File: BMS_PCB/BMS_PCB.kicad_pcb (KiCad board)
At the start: 2 copper layers, 163 parts, among them IC1 TPS560430XFDBVT, IC3 AMC1350DWVR, IC4 AMC1350DWVR, IC5 AMC1350DWVR, IC6 AMC1350DWVR, J1 Conn_01x37, J2 Conn_01x09, K1 Relay_SPST-NO, Q1 2N7002KT7G, U1 TLV2404IDR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

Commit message: Update BMS_PCB.kicad_pcb
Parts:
- moved J1 5.75 mm to (212.9, 130.6), turned to 90 degrees

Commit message: test
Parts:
- moved J1 99.5 mm to (239.2, 34.6)
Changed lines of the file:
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@@
 	(footprint "Connector_Dsub:DSUB-37_Socket_Horizontal_P2.77x2.84mm_EdgePinOffset14.56mm_Housed_MountingHolesOffset15.98mm"
 		(layer "F.Cu")
-		(at 212.925 130.58 90)
+		(at 239.159669 34.575 90)
 		(descr "37-pin D-Sub connector, horizontal/angled (90 deg), THT-mount, socket (female), pitch 2.77x2.84mm, pin-PCB-offset 14.56mm, distance of mounting holes 63.5mm, distance of mounting holes to PCB edge 15.98mm, see https://disti-assets.s3.amazonaws.com/tonar/files/datasheets/16730.pdf")
 		(tags "37-pin D-Sub connector horizontal angled 90deg THT socket pitch 2.77x2.84mm pin-PCB-offset 14.56mm mounting-holes-distance 63.5mm mounting-hole-offset 15.98mm")

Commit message: Update BMS_PCB.kicad_pcb
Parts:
- moved F5 93.1 mm to (271.0, 49.0), turned to 90 degrees
- moved R1 72.0 mm to (244.7, 70.3), turned to 180 degrees
- moved C18 71.0 mm to (273.0, 40.5), turned to 90 degrees
- moved C21 70.6 mm to (270.6, 31.0), turned to 180 degrees
- moved L1 68.7 mm to (271.0, 35.5), turned to 90 degrees
- moved C11 68.6 mm to (241.7, 65.3), turned to 90 degrees
- moved C19 68.2 mm to (270.0, 40.5), turned to 90 degrees
- moved C14 68.1 mm to (242.0, 77.9), turned to 90 degrees
- moved C5 67.8 mm to (241.8, 71.5), turned to -90 degrees
- moved PS1 67.6 mm to (253.5, 42.0), turned to 180 degrees
- moved R2 67.0 mm to (244.8, 72.5), turned to 180 degrees
- moved R8 66.8 mm to (244.7, 66.3), turned to 180 degrees
- moved R6 66.7 mm to (244.7, 64.3), turned to 180 degrees
- moved C1 65.1 mm to (239.0, 68.0)
- moved R10 62.8 mm to (239.7, 65.3), turned to 90 degrees
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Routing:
- net +BATT: track 0.00 -> 96.2 mm
- net -BATT: track 0.00 -> 58.0 mm
- net 12V_DCDC: track 0.00 -> 51.0 mm
- net Net-(PS1--VIN): track 0.00 -> 40.0 mm
- net Net-(PS1-+VIN): track 0.00 -> 14.5 mm
- net Net-(U1C-+): track 0.00 -> 10.1 mm
- net Net-(U1D-+): track 0.00 -> 10.1 mm
- net Net-(U1A-+): track 0.00 -> 9.40 mm
- net Net-(U2A-+): track 0.00 -> 9.40 mm
- net Net-(U2B-+): track 0.00 -> 9.22 mm
- net Net-(U1B-+): track 0.00 -> 9.03 mm
- net Relais_in+: track 0.00 -> 8.04 mm
- net +5V: track 0.00 -> 5.84 mm
- net Net-(U1C--): track 0.00 -> 4.94 mm
- net Net-(U1D--): track 0.00 -> 4.79 mm
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
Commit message: Freitag
Ich habe heute viele Bauteile zusammengesetzt. Die Leiterbahnen würde ich eher zum Schluss machen.
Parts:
- moved C2 146.6 mm to (210.8, 100.1), turned to 90 degrees
- moved C4 144.9 mm to (210.3, 107.1), turned to -90 degrees
- moved C15 142.9 mm to (210.8, 129.5), turned to 90 degrees
- moved C16 141.5 mm to (210.3, 137.1), turned to -90 degrees
- moved C6 140.8 mm to (205.3, 107.1), turned to 90 degrees
- moved C43 139.8 mm to (210.8, 114.6), turned to 90 degrees
- moved C44 138.2 mm to (210.3, 122.0), turned to -90 degrees
- moved C10 137.2 mm to (199.8, 107.1), turned to -90 degrees
- moved C17 137.0 mm to (205.3, 137.1), turned to 90 degrees
- moved C47 134.6 mm to (205.3, 122.0), turned to 90 degrees
- moved C63 132.2 mm to (210.8, 144.5), turned to 90 degrees
- moved C8 131.2 mm to (194.3, 107.1), turned to 90 degrees
- moved C64 131.1 mm to (210.3, 152.1), turned to -90 degrees
- moved C49 130.7 mm to (199.8, 122.1), turned to -90 degrees
- moved C12 128.4 mm to (189.3, 107.1), turned to 90 degrees
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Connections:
- K1 pad 1: (no net) -> Net-(K1-Pad14)
- K1 pad 2: (no net) -> Net-(D2-A)
- K1 pad 4: (no net) -> Precharge_out
- K1 pad 5: (no net) -> +5V
- K1 pad 6: (no net) -> Net-(K1-Pad14)
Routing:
- net GND: track 0.14 -> 38.3 mm
- net Net-(D2-A): track 0.00 -> 19.7 mm
- net Net-(U11A--): track 0.00 -> 16.8 mm
- net Net-(U11B--): track 0.00 -> 16.2 mm
- net Current: track 0.00 -> 16.1 mm
- net Net-(U11B-+): track 0.00 -> 12.3 mm
- net Net-(U11A-+): track 0.00 -> 12.1 mm
- net Net-(U8--): track 0.00 -> 10.9 mm
- net +5V: track 5.84 -> 16.5 mm
- net Net-(U8-+): track 0.00 -> 7.71 mm
- net Net-(Q1-G): track 0.00 -> 5.83 mm
- net Precharge_uC: track 0.00 -> 5.62 mm
- net Vcc_Current: track 0.00 -> 4.82 mm
- net Net-(C51-Pad2): track 0.00 -> 3.09 mm
- net Net-(C31-Pad2): track 0.00 -> 3.09 mm

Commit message: Sonntag
Ich habe das Layout weitergemacht, die restlichen Schaltungen zusammengestellt und das meiste bereits verbunden.  Problem sind noch die PS-Boxen (R1SE-0505-R), die für die Voltage Messung noch angeschlossen werden müssen. da müssen wir schauen, wie wir die platztechnisch platzieren.
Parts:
- moved PS6 166.6 mm to (205.2, 93.6)
- moved C59 161.9 mm to (194.5, 93.0), turned to -90 degrees
- moved U10 154.7 mm to (224.2, 50.5)
- moved PS5 153.2 mm to (205.2, 76.9)
- moved C55 149.9 mm to (194.5, 77.4), turned to -90 degrees
- moved PS4 143.9 mm to (205.2, 60.4)
- moved C53 142.9 mm to (194.5, 60.5), turned to -90 degrees
- moved C52 139.0 mm to (194.5, 45.5), turned to -90 degrees
- moved PS3 138.8 mm to (205.2, 44.0)
- moved J2 105.9 mm to (141.9, 130.2)
- moved U7 88.7 mm to (153.5, 72.5)
- moved C39 85.0 mm to (196.8, 131.0)
- moved C40 75.7 mm to (190.2, 147.5), turned to 90 degrees
- moved IC1 64.0 mm to (226.3, 35.0)
- moved C42 62.2 mm to (175.0, 134.0), turned to 90 degrees
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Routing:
- net GND: track 38.3 -> 169.1 mm
- net +5V: track 16.5 -> 86.7 mm
- net Net-(U3A--): track 0.00 -> 55.5 mm
- net Net-(U3A-+): track 0.00 -> 47.2 mm
- net Voltage1: track 0.00 -> 43.8 mm
- net Voltage3: track 0.00 -> 43.3 mm
- net Voltage2: track 0.00 -> 42.0 mm
- net Net-(U3B-+): track 0.00 -> 31.0 mm
- net Net-(U3B--): track 0.00 -> 30.3 mm
- net Net-(U3D-+): track 0.00 -> 28.0 mm
- net Voltage0: track 0.00 -> 27.7 mm
- net Net-(U3C--): track 0.00 -> 26.8 mm
- net Net-(U3C-+): track 0.00 -> 25.8 mm
- net Voltage23_uC: track 0.00 -> 25.6 mm
- net Net-(C31-Pad2): track 3.09 -> 27.9 mm
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
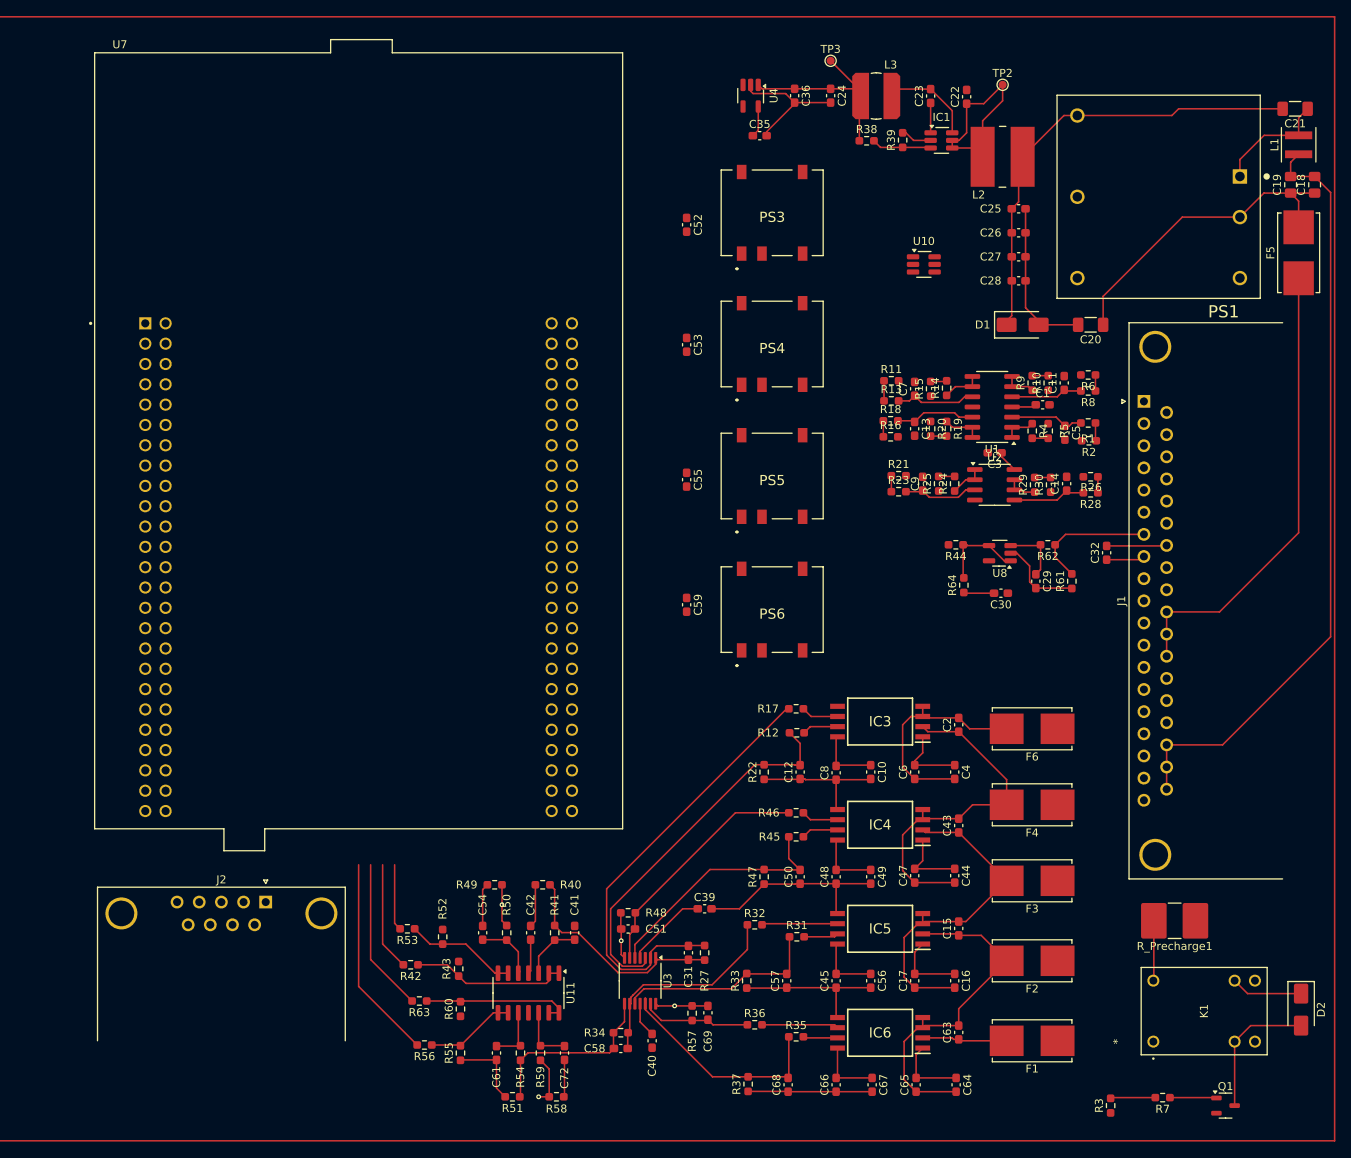
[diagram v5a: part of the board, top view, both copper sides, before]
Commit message: Montag, 28.04.
Pin Belegung PCB geändert, noch nicht in Schematics
PS-Boxen platziert
80 % fertig verteilt und verbunden
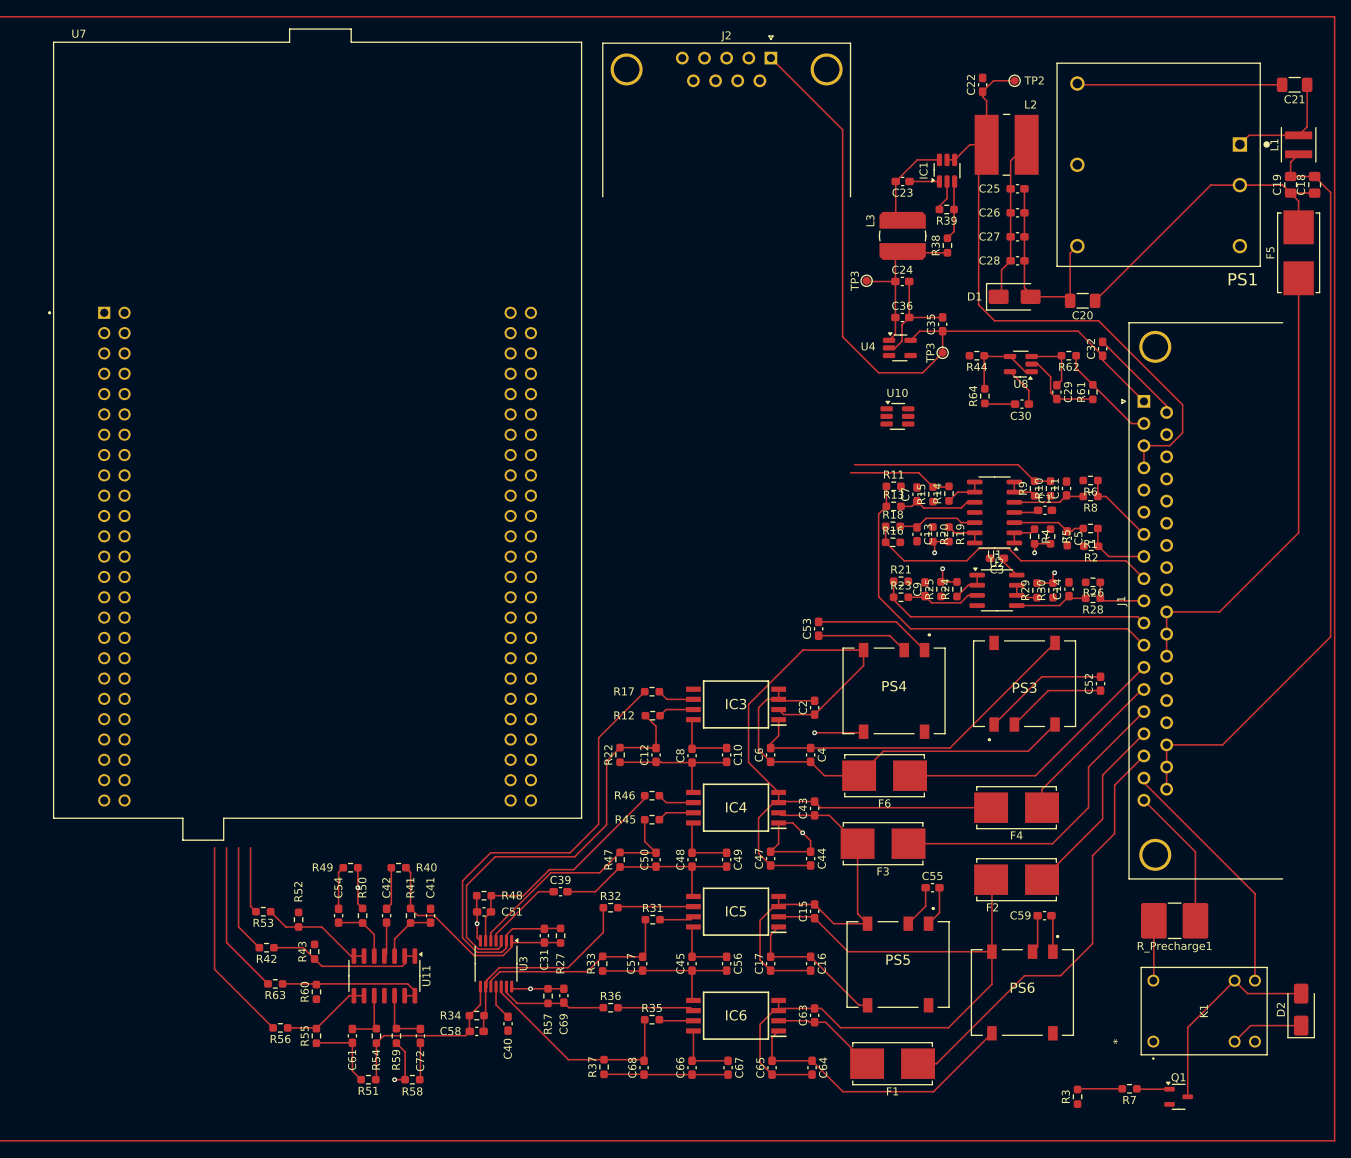
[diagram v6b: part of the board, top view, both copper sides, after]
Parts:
- added TP3: TestPoint, TestPoint:TestPoint_Pad_D1.0mm, F.Cu at (226.5, 61.5)
- moved J2 123.0 mm to (205.0, 24.7)
- moved C52 77.2 mm to (246.2, 102.9), turned to 90 degrees
- moved PS3 66.8 mm to (236.7, 102.9)
- moved PS5 63.1 mm to (220.9, 138.0), turned to 180 degrees
- moved C55 59.5 mm to (225.2, 128.4), turned to 0 degrees
- moved C59 59.3 mm to (239.2, 131.9), turned to 0 degrees
- moved PS6 57.2 mm to (236.5, 141.5), turned to 180 degrees
- moved PS4 46.0 mm to (220.4, 103.8), turned to 180 degrees
- moved C53 39.1 mm to (211.0, 96.0), turned to 90 degrees
- moved U4 36.6 mm to (221.2, 60.9), turned to 0 degrees
- moved C35 32.8 mm to (226.5, 57.9), turned to 90 degrees
- moved C36 30.8 mm to (221.5, 57.1), turned to 0 degrees
- moved TP3 27.9 mm to (217.0, 52.5), turned to 90 degrees
- moved C32 25.5 mm to (246.5, 61.0)
- moved C24 24.9 mm to (221.5, 52.6), turned to 0 degrees
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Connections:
- F1 pad 1: Net-(J1-Pin_13) -> Net-(J1-Pin_17)
- F2 pad 1: Net-(J1-Pin_12) -> Net-(J1-Pin_16)
- F3 pad 1: Net-(J1-Pin_11) -> Net-(J1-Pin_15)
- F4 pad 1: Net-(J1-Pin_10) -> Net-(J1-Pin_14)
- F6 pad 1: Net-(J1-Pin_9) -> Net-(J1-Pin_13)
- J1 pad 1: Temp1 -> Vcc_Current
- J1 pad 10: Net-(J1-Pin_10) -> Temp6
- J1 pad 11: Net-(J1-Pin_11) -> Temp5
- J1 pad 12: Net-(J1-Pin_12) -> Temp3
- J1 pad 14: Precharge_out -> Net-(J1-Pin_14)
- J1 pad 15: Precharge_in -> Net-(J1-Pin_15)
- J1 pad 16: Relais_out+ -> Net-(J1-Pin_16)
- J1 pad 17: Relais_in+ -> Net-(J1-Pin_17)
- J1 pad 18: Relais_out- -> Precharge_out
- J1 pad 19: Relais_in+ -> Precharge_in
- J1 pad 2: Temp2 -> Current
- J1 pad 3: Temp3 -> Relais_in+
- J1 pad 4: Temp4 -> Relais_in+
- J1 pad 5: Temp5 -> Relais_out+
- J1 pad 6: Temp6 -> Relais_out-
- J1 pad 7: Current -> Temp2
- J1 pad 8: Vcc_Current -> Temp1
- J1 pad 9: Net-(J1-Pin_9) -> Temp4
- K1 pad 2: Net-(D2-A) -> +5V
- K1 pad 5: +5V -> Net-(D2-A)
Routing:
- net Vcc_Current: track 8.75 -> 90.2 mm
- net Relais_in+: track 26.6 -> 81.6 mm
- net Net-(J1-Pin_17): track 0.00 -> 54.2 mm
- net GND: track 169.1 -> 216.6 mm
- net Temp3: track 2.51 -> 49.9 mm
- net Voltage3: track 43.3 -> 87.8 mm
- net Voltage1: track 43.8 -> 88.2 mm
- net Net-(J1-Pin_15): track 0.00 -> 39.2 mm
- net +5V_Bat0: track 8.96 -> 45.0 mm
- net Temp4: track 2.00 -> 37.4 mm
- net Net-(J1-Pin_13): track 0.00 -> 34.8 mm
- net +5V: track 86.7 -> 121.5 mm
- net Temp5: track 2.00 -> 34.8 mm
- net Precharge_out: track 0.00 -> 31.1 mm
- net Voltage0: track 27.7 -> 55.1 mm
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
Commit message: Footprints changes
-U10
-uC pins/SPI changes
- Fuses
- DSUB
- reupload layout
- etc.
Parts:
- removed the TP3 at (217.0, 52.5)
- removed the TP3 at (226.5, 61.5)
- added R65: DUMMY, Resistor_SMD:R_0603_1608Metric_Pad0.98x0.95mm_HandSolder, F.Cu at (72.7, 65.2)
- added TP1: TestPoint, TestPoint:TestPoint_Pad_D1.0mm, F.Cu at (72.0, 70.0)
- added TP3: TestPoint, TestPoint:TestPoint_Pad_D1.0mm, F.Cu at (72.0, 57.0)
- C22: value 2,2u -> 2u2
- F1, F2, F3, F4, F6: value 1A -> 100mA; footprint Fuse:Fuseholder_Littelfuse_Nano2_154x -> Fuse:Fuse_Littelfuse-NANO2-451_453
- J2: value Conn_01x09 -> Conn_01x15; footprint Connector_Dsub:DSUB-9_Socket_Horizontal_P2.77x2.84mm_EdgePinOffset14.56mm_Housed_MountingHolesOffset15.98mm -> Connector_Dsub:DSUB-15_Socket_Horizontal_P2.77x2.84mm_EdgePinOffset14.56mm_Housed_MountingHolesOffset15.98mm
- K1: value Relay_SPST-NO -> J1021AS35VDC.20
- R44: value 1k -> 100
- U10: footprint Package_TO_SOT_SMD:SOT-23-6_Handsoldering -> Package_SO:SOIC-16_3.9x9.9mm_P1.27mm
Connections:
- F1 pad 1: Net-(J1-Pin_17) -> Net-(J1-Pin_13)
- F2 pad 1: Net-(J1-Pin_16) -> Net-(J1-Pin_12)
- F3 pad 1: Net-(J1-Pin_15) -> Net-(J1-Pin_11)
- F4 pad 1: Net-(J1-Pin_14) -> Net-(J1-Pin_10)
- F6 pad 1: Net-(J1-Pin_13) -> Net-(J1-Pin_9)
- J1 pad 1: Vcc_Current -> Temp1
- J1 pad 10: Temp6 -> Net-(J1-Pin_10)
- J1 pad 11: Temp5 -> Net-(J1-Pin_11)
- J1 pad 12: Temp3 -> Net-(J1-Pin_12)
- J1 pad 14: Net-(J1-Pin_14) -> Precharge_out
- J1 pad 15: Net-(J1-Pin_15) -> Precharge_in
- J1 pad 16: Net-(J1-Pin_16) -> Relais_out+
- J1 pad 17: Net-(J1-Pin_17) -> Relais_in+
- J1 pad 18: Precharge_out -> Relais_out-
- J1 pad 19: Precharge_in -> Relais_in+
- J1 pad 2: Current -> Temp2
- J1 pad 3: Relais_in+ -> Temp3
- J1 pad 4: Relais_in+ -> Temp4
- J1 pad 5: Relais_out+ -> Temp5
- J1 pad 6: Relais_out- -> Temp6
- J1 pad 7: Temp2 -> Current
- J1 pad 8: Temp1 -> Vcc_Current
- J1 pad 9: Temp4 -> Net-(J1-Pin_9)
- J2 pad 8: unconnected-(J2-Pin_8-Pad8) -> Touchdisplay_x
- J2 pad 9: unconnected-(J2-Pin_9-Pad9) -> Touchdisplay_y
- K1 pad 1: Net-(K1-Pad14) -> Net-(K1-Pad1)
- K1 pad 3: (no net) -> unconnected-(K1-Pad3)
- K1 pad 6: Net-(K1-Pad14) -> unconnected-(K1-Pad6)
- R44 pad 1: Net-(U8--) -> Net-(R44-Pad1)
- R64 pad 2: Net-(U8--) -> Net-(R44-Pad1)
- R_Precharge1 pad 2: Net-(K1-Pad14) -> Net-(K1-Pad1)
- U7 pad P1_18: unconnected-(U7A-PA6-PadP1_18) -> Touchdisplay_x
- U7 pad P1_19: Current_uC -> Temp3_uC
- U7 pad P1_7: Temp3_uC -> Current_uC
- U7 pad P1_8: unconnected-(U7A-PC0-PadP1_8) -> Touchdisplay_y
- U7 pad P2_11: unconnected-(U7B-PE6-PadP2_11) -> Touchdisplay_y-
- U7 pad P2_13: unconnected-(U7B-PE4-PadP2_13) -> Touchdisplay_x-
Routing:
- net (no net): track 0.00 -> 146.7 mm
- net Net-(J1-Pin_17): track 54.2 -> 0.00 mm
- net Net-(J1-Pin_15): track 39.2 -> 0.00 mm
- net Net-(J1-Pin_16): track 23.8 -> 0.00 mm
- net Net-(J1-Pin_14): track 22.0 -> 0.00 mm
- net Net-(K1-Pad14): track 7.51 -> 0.00 mm

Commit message: Dienstag, 29.04.
Layout soweit fertig gestellt, Probleme noch mit Footprints
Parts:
- moved TP3 162.0 mm to (234.0, 57.5), turned to 90 degrees
- moved TP1 147.0 mm to (218.5, 57.5)
- moved R65 136.0 mm to (208.5, 72.1), turned to 180 degrees
- moved J2 46.5 mm to (250.7, 33.8), turned to 90 degrees
- moved IC1 36.8 mm to (198.9, 62.5), turned to 180 degrees
- moved L2 32.5 mm to (202.0, 37.0)
- moved C21 31.7 mm to (239.0, 31.5)
- moved C18 31.6 mm to (241.5, 42.0)
- moved C19 31.6 mm to (238.5, 42.0)
- moved C20 31.6 mm to (212.5, 56.5)
- moved C25 31.6 mm to (204.3, 42.5)
- moved C26 31.6 mm to (204.3, 45.5)
- moved C27 31.6 mm to (204.3, 48.5)
- moved C28 31.6 mm to (204.3, 51.5)
- moved D1 31.6 mm to (204.0, 56.0)
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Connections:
- F1 pad 1: Net-(J1-Pin_13) -> Net-(J1-Pin_17)
- F2 pad 1: Net-(J1-Pin_12) -> Net-(J1-Pin_16)
- F3 pad 1: Net-(J1-Pin_11) -> Net-(J1-Pin_15)
- F4 pad 1: Net-(J1-Pin_10) -> Net-(J1-Pin_14)
- F6 pad 1: Net-(J1-Pin_9) -> Net-(J1-Pin_13)
- J1 pad 1: Temp1 -> Vcc_Current
- J1 pad 10: Net-(J1-Pin_10) -> Temp6
- J1 pad 11: Net-(J1-Pin_11) -> Temp5
- J1 pad 12: Net-(J1-Pin_12) -> Temp3
- J1 pad 14: Precharge_out -> Net-(J1-Pin_14)
- J1 pad 15: Precharge_in -> Net-(J1-Pin_15)
- J1 pad 16: Relais_out+ -> Net-(J1-Pin_16)
- J1 pad 17: Relais_in+ -> Net-(J1-Pin_17)
- J1 pad 18: Relais_out- -> Precharge_out
- J1 pad 19: Relais_in+ -> Precharge_in
- J1 pad 2: Temp2 -> Relais_in+
- J1 pad 3: Temp3 -> Relais_in+
- J1 pad 4: Temp4 -> Relais_out+
- J1 pad 5: Temp5 -> Relais_out-
- J1 pad 6: Temp6 -> Current
- J1 pad 7: Current -> Temp2
- J1 pad 8: Vcc_Current -> Temp1
- J1 pad 9: Net-(J1-Pin_9) -> Temp4
- K1 pad 1: Net-(K1-Pad1) -> (no net)
- K1 pad 6: unconnected-(K1-Pad6) -> Net-(K1-Pad1)
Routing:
- net +5V: track 121.5 -> 456.8 mm, vias 0 -> 20
- net GND: track 216.6 -> 16.8 mm
- net (no net): track 146.7 -> 0.00 mm
- net Precharge_uC: track 5.62 -> 129.6 mm, vias 0 -> 1
- net Touchdisplay_x-: track 0.00 -> 65.0 mm, vias 0 -> 1
- net Touchdisplay_y: track 0.00 -> 63.8 mm, vias 0 -> 1
- net Touchdisplay_y-: track 0.00 -> 63.6 mm, vias 0 -> 1
- net Display_MOSI: track 0.00 -> 61.6 mm, vias 0 -> 1
- net Display_CLK: track 0.00 -> 61.4 mm, vias 0 -> 1
- net Touchdisplay_x: track 0.00 -> 61.4 mm, vias 0 -> 1
- net Display_RST: track 0.00 -> 61.1 mm, vias 0 -> 1
- net Display_D/C: track 0.00 -> 60.8 mm, vias 0 -> 1
- net Display_CS: track 0.00 -> 60.7 mm, vias 0 -> 1
- net Relais_uC: track 0.00 -> 57.6 mm, vias 0 -> 1
- net Relais_in+: track 81.6 -> 133.9 mm
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- added copper zone on B.Cu, net GND
- added copper zone on F.Cu, net GND
